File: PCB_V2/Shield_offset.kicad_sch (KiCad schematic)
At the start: 96 parts, among them J1 ADC, J10 I2C, J11 SERVO3, J12 SERVO4, J13 Power OUT, J2 BATT, J4 Screw_Terminal_01x04, J5 SERVO1, J6 ULTRA, J7 ENC1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

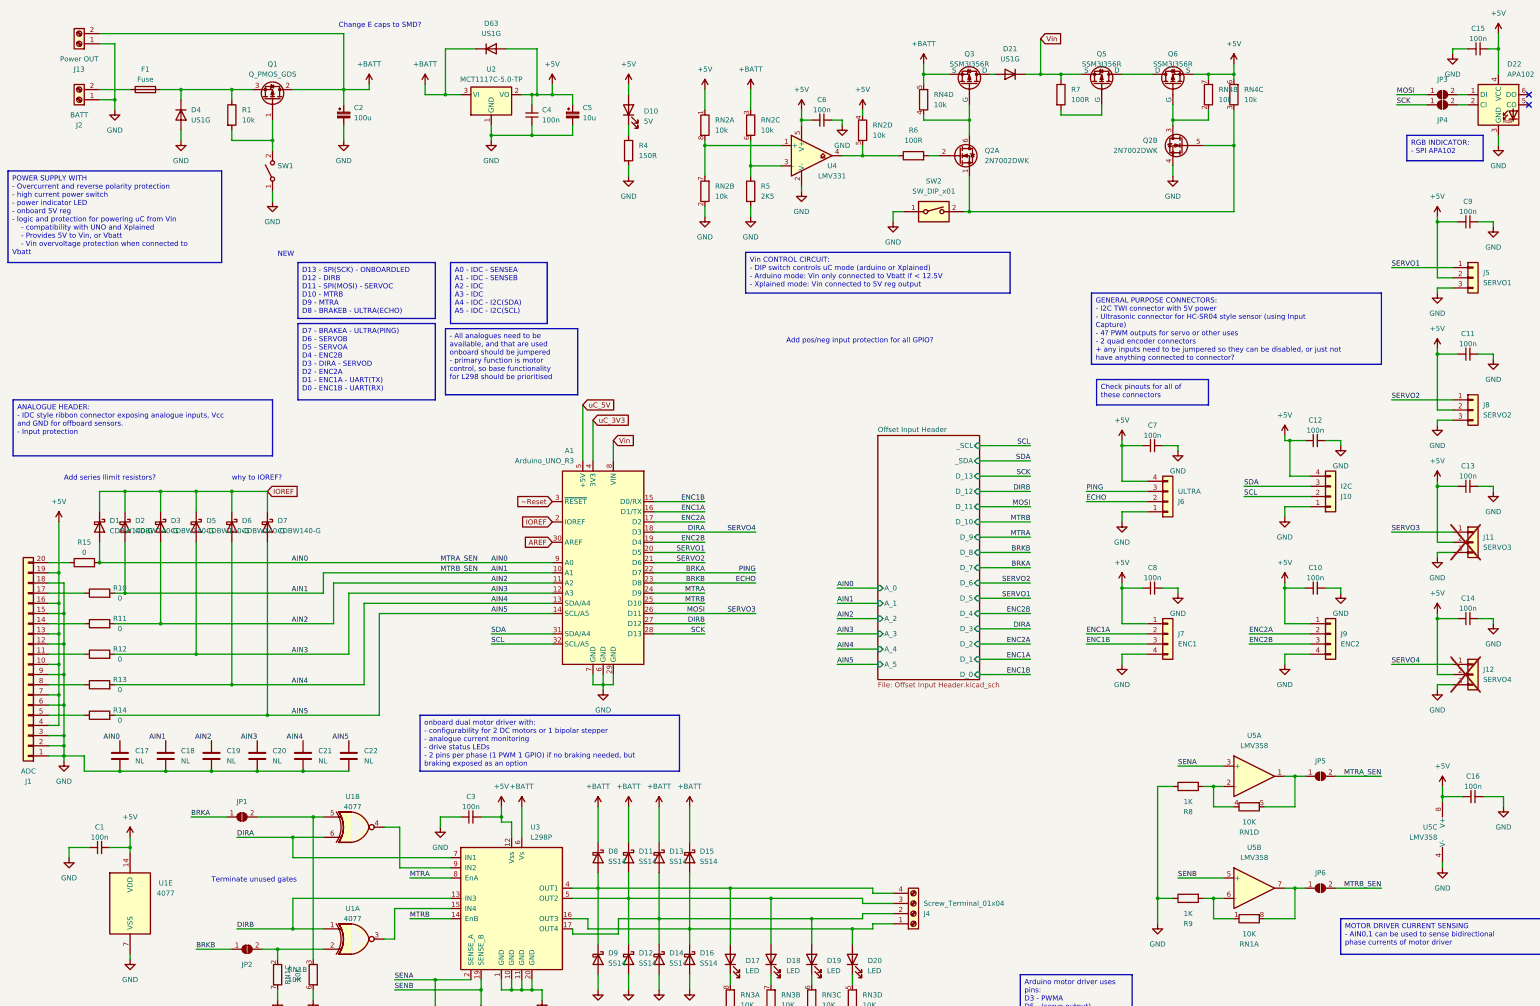
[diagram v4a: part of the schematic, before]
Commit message: Tidied schematic and removed old comments
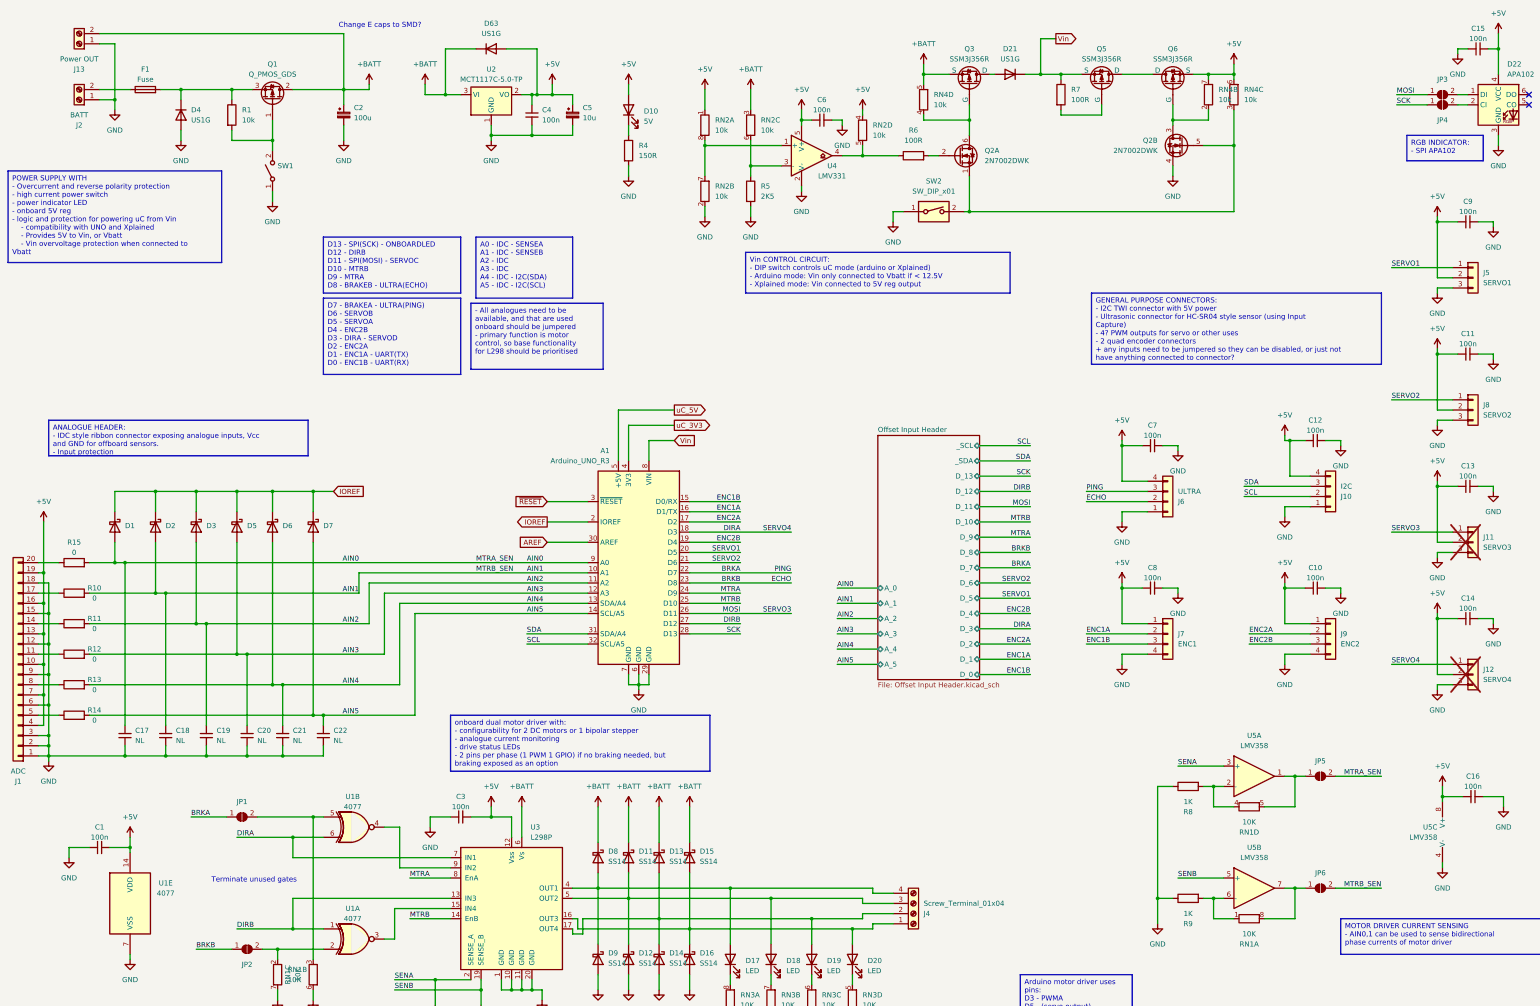
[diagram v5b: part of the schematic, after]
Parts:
- C17, C18, C19, C20, C21, C22: symbol Device:C -> Device:C_Small
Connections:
- net ~Reset renamed ~{RESET}
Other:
- note removed: "Add pos/neg input protection for all GPIO?"
- note removed: "Add series Ilimit resistors?"
- note removed: "NEW"
- note removed: "why to IOREF?"
- moved on the sheet: A1, C17, C18, C19, C20, C21, C22, C3, D1, D2, D3, D5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

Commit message: Changed to vertical connector
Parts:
- J1: footprint Connector_IDC:IDC-Header_2x10_P2.54mm_Horizontal -> Connector_IDC:IDC-Header_2x10_P2.54mm_Vertical
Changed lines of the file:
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@@
       (effects (font (size 1.27 1.27)))
     )
-    (property "Footprint" "Connector_IDC:IDC-Header_2x10_P2.54mm_Horizontal" (at 19.05 176.53 0)
+    (property "Footprint" "Connector_IDC:IDC-Header_2x10_P2.54mm_Vertical" (at 19.05 176.53 0)
       (effects (font (size 1.27 1.27)) hide)
     )

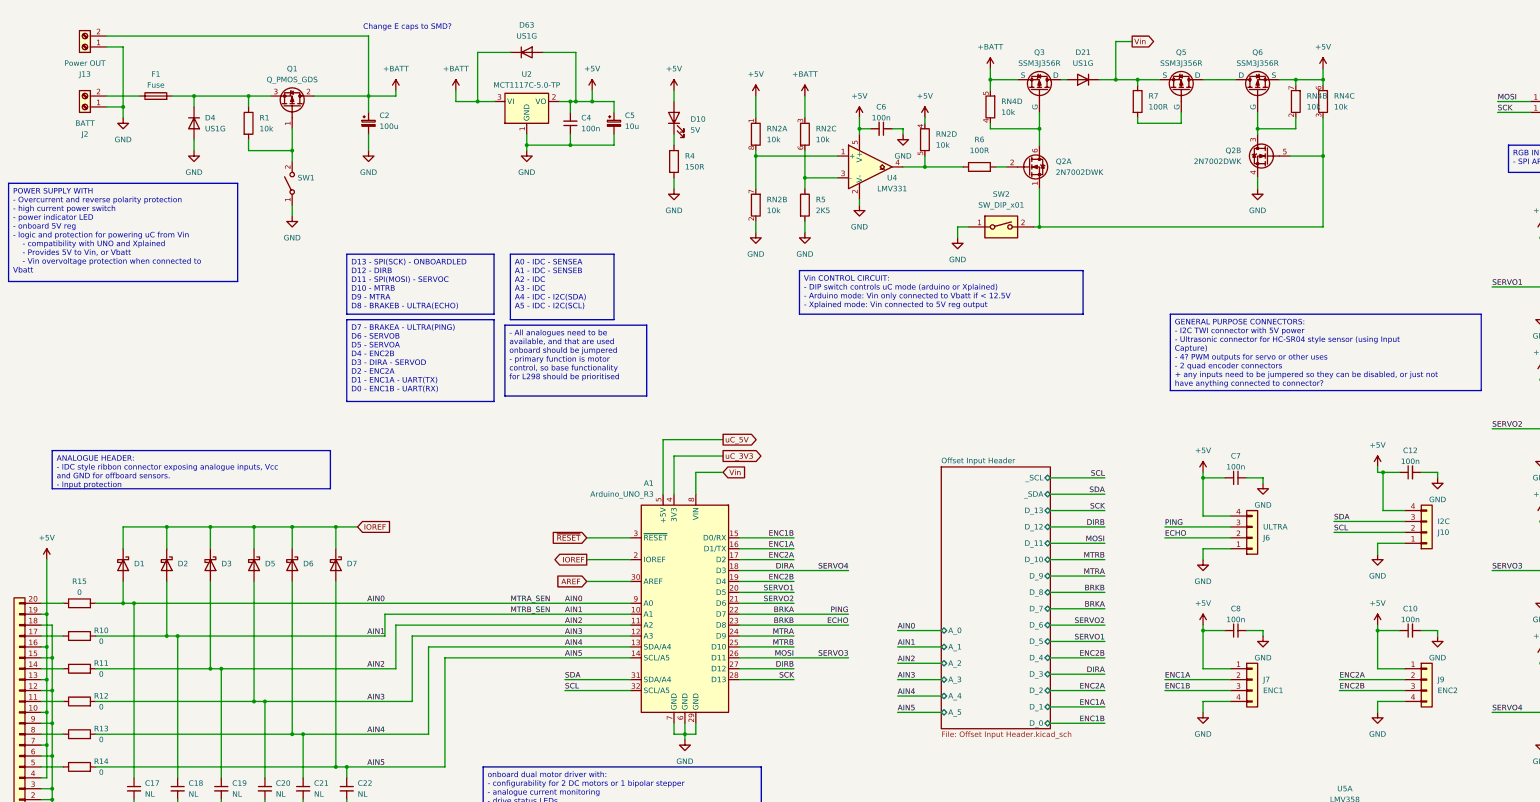
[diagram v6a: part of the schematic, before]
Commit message: Swapped ENC1 and ENC2 so they match the motor they are next to
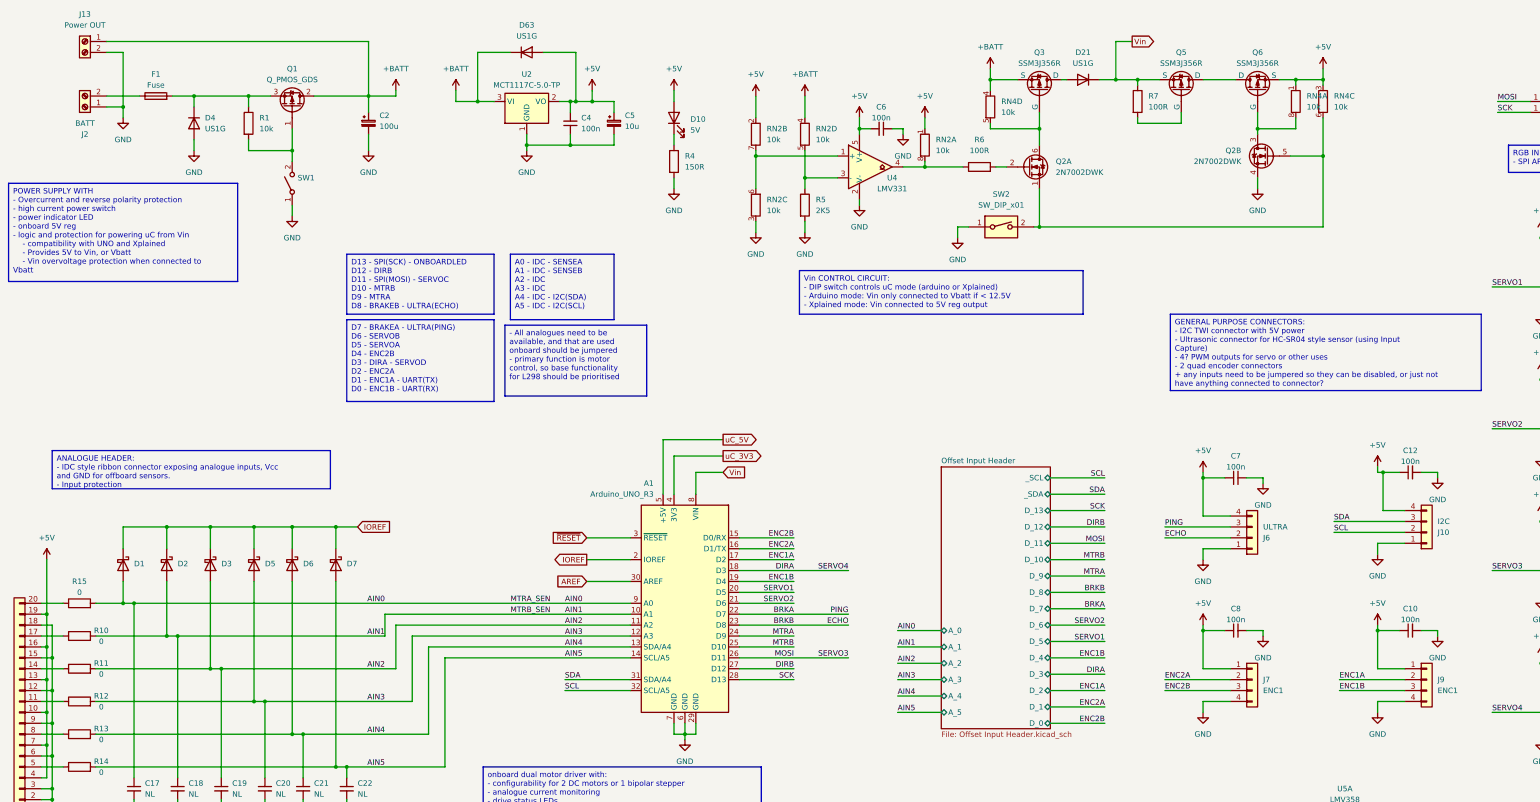
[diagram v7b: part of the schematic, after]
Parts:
- J9: value ENC2 -> ENC1
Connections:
- net +5V: now also RN2.2 (R2.1), RN4.1 (R1.1), RN4.3 (R3.1); no longer RN2.4 (R4.1), RN4.6 (R3.2), RN4.7 (R2.2)
- net +BATT: now also J13.1 (Pin_1), RN2.4 (R4.1), RN4.4 (R4.1); no longer J13.2 (Pin_2), RN2.3 (R3.1), RN4.5 (R4.2)
- net ENC1A: now also A1.17 (D2), J9.2 (Pin_2); no longer A1.16 (D1/TX), J7.2 (Pin_2)
- net ENC1B: now also A1.19 (D4), J9.3 (Pin_3); no longer A1.15 (D0/RX), J7.3 (Pin_3)
- net ENC2A: now also A1.16 (D1/TX), J7.2 (Pin_2); no longer A1.17 (D2), J9.2 (Pin_2)
- net ENC2B: now also A1.15 (D0/RX), J7.3 (Pin_3); no longer A1.19 (D4), J9.3 (Pin_3)
- net GND: now also J13.2 (Pin_2), RN2.3 (R3.1); no longer J13.1 (Pin_1), RN2.2 (R2.1)
- net at Q2.1 (S), Q2.5 (G), SW2.2: now also RN4.6 (R3.2); no longer RN4.3 (R3.1)
- net at Q2.6 (D), Q3.1 (G): now also RN4.5 (R4.2); no longer RN4.4 (R4.1)
- net at R5.1, U4.3 (-): now also RN2.5 (R4.2); no longer RN2.6 (R3.2)
- net at RN2.7 (R2.2), U4.1 (+): now also RN2.6 (R3.2); no longer RN2.8 (R1.2)
- net at R6.1, U4.4: now also RN2.8 (R1.2); no longer RN2.5 (R4.2)
- net at Q2.3 (D), Q6.1 (G): now also RN4.8 (R1.2); no longer RN4.2 (R2.1)
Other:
- note removed: "Change E caps to SMD?"
- moved on the sheet: J13, RN4A, RN4C, RN4D
